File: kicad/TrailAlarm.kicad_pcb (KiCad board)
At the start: 2 copper layers, 71.1 x 36.2 mm, 57 parts, among them IC1 MAX865EUA+T, J1 Conn_01x03, J2 Conn_01x01_Male, J3 Adafruit ADS1115, J4 Bat, Q1 2N3904, SW1 SW_DIP_x01, U1 TLC274, U2 TL074, U3 PocketBeagle, U5 AD620

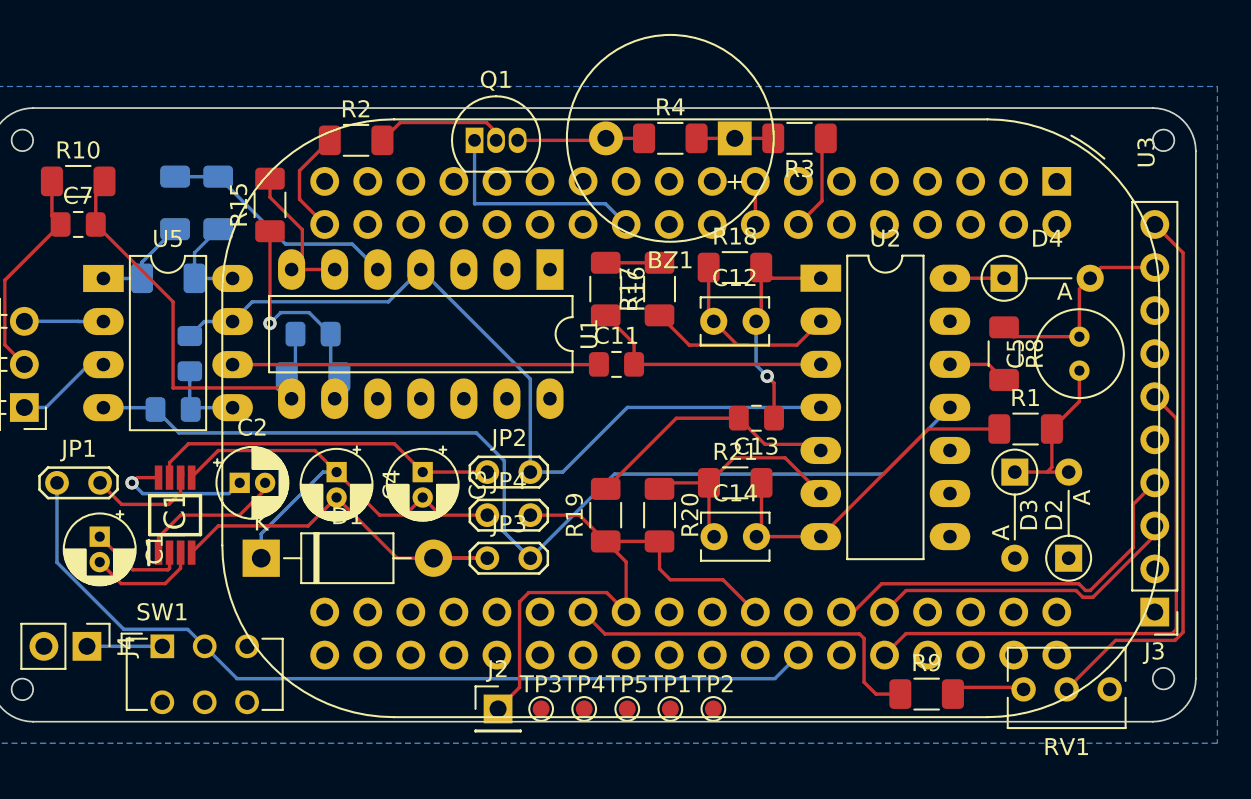
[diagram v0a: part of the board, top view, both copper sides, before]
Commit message: Done Layout
- Add paths for test points, better ground plane
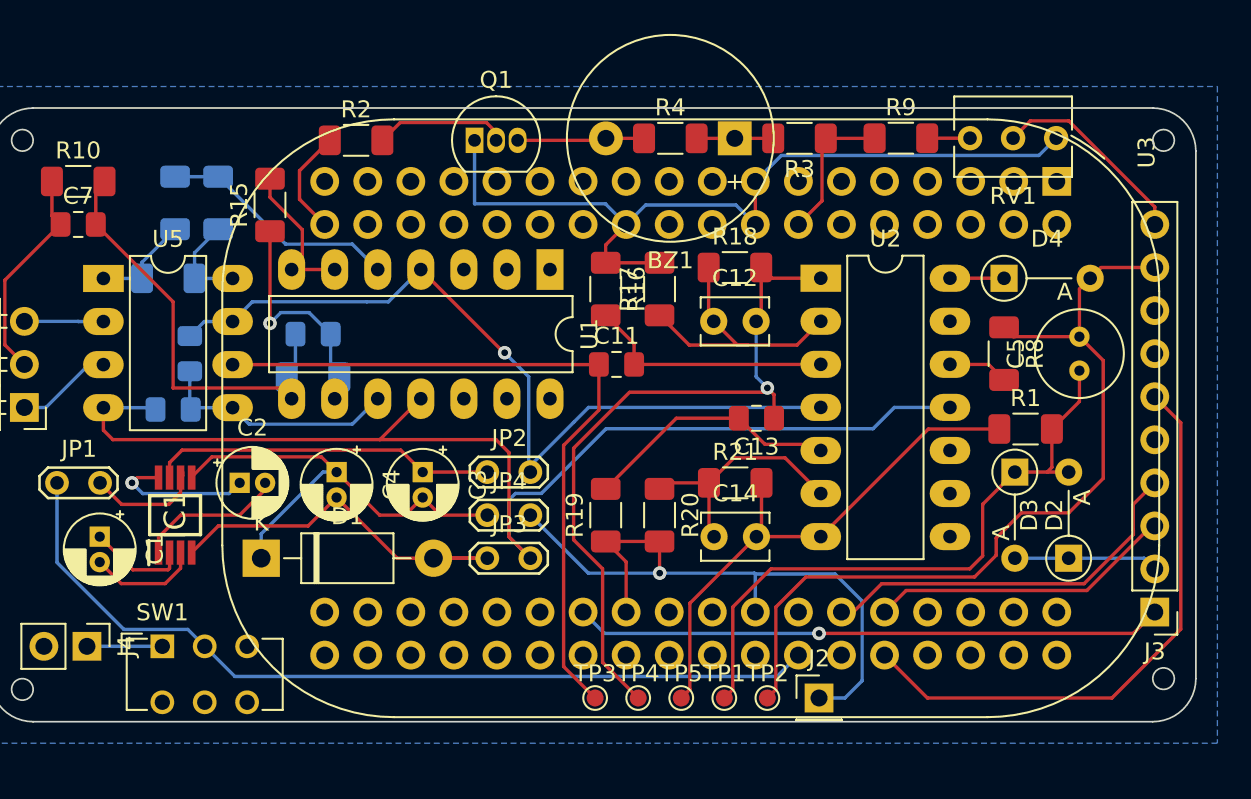
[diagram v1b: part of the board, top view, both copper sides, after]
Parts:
- moved R9 32.8 mm to (169.9, 14.5)
- moved RV1 32.7 mm to (174.0, 14.5)
- moved J2 18.9 mm to (165.1, 47.5)
- moved TP1 3.25 mm to (159.5, 47.5)
- moved TP2 3.25 mm to (162.1, 47.5)
- moved TP3 3.25 mm to (151.9, 47.5)
- moved TP4 3.25 mm to (154.4, 47.5)
- moved TP5 3.25 mm to (157.0, 47.5)
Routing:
- net GND: track 59.2 -> 113.6 mm, vias 0 -> 1
- net TO_ADC: track 12.8 -> 50.4 mm
- net Net-(C12-Pad2): track 13.2 -> 42.4 mm
- net Net-(C5-Pad1): track 10.3 -> 37.6 mm
- net Net-(C11-Pad1): track 21.6 -> 42.9 mm
- net Vref_mid: track 33.0 -> 11.9 mm
- net +3V3: track 28.0 -> 43.4 mm, vias 0 -> 1
- net VS: track 59.8 -> 71.3 mm
- net /EEG Amplifer/FullSignal: track 20.3 -> 31.6 mm
- net ~{ADC_RDY}: track 32.1 -> 34.5 mm
- net Vref_top: track 4.38 -> 2.53 mm
- net I2C_SDA: track 23.5 -> 22.7 mm
- net I2C_SCL: track 18.7 -> 18.0 mm
- net VD: track 48.6 -> 48.8 mm, vias 0 -> 1

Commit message: Export gerber files
- Reflow
- print to pdf
- generate gerber/drill files for fab
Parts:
- moved BZ1 99.8 mm to (160.8, 114.3)
- moved C1 99.8 mm to (123.4, 137.8)
- moved C11 99.8 mm to (153.9, 127.6)
- moved C12 99.8 mm to (159.6, 125.1)
- moved C14 99.8 mm to (159.6, 137.8)
- moved C3 99.8 mm to (142.4, 134.0)
- moved C4 99.8 mm to (137.4, 134.0)
- moved C7 99.8 mm to (122.1, 119.4)
- moved C8 99.8 mm to (136.0, 125.9)
- moved C9 99.8 mm to (128.7, 127.0)
- moved D1 99.8 mm to (132.9, 139.1)
- moved D2 99.8 mm to (177.4, 134.0)
- moved D3 99.8 mm to (180.5, 139.1)
- moved D4 99.8 mm to (176.7, 122.6)
- moved J1 99.8 mm to (118.9, 130.2)
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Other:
- outline, holes or cut-outs redrawn

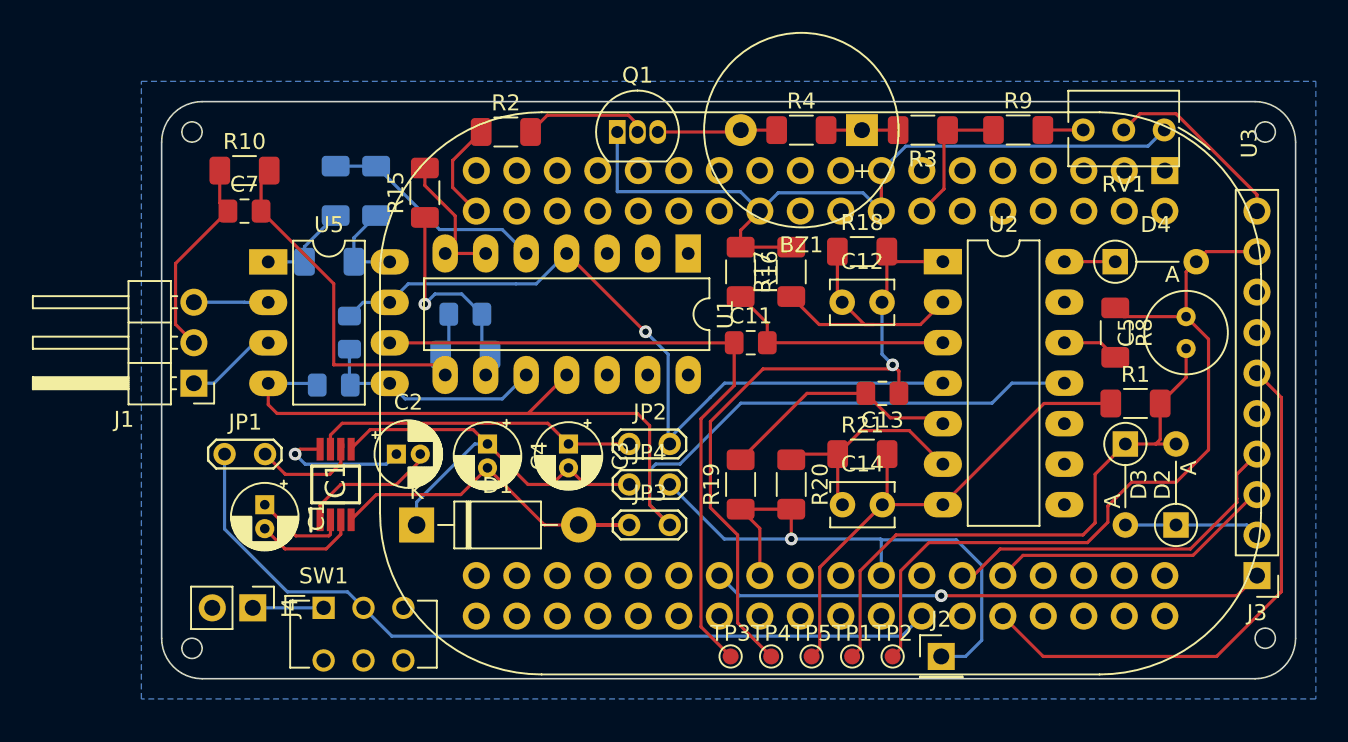
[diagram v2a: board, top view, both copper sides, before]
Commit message: Updated layout
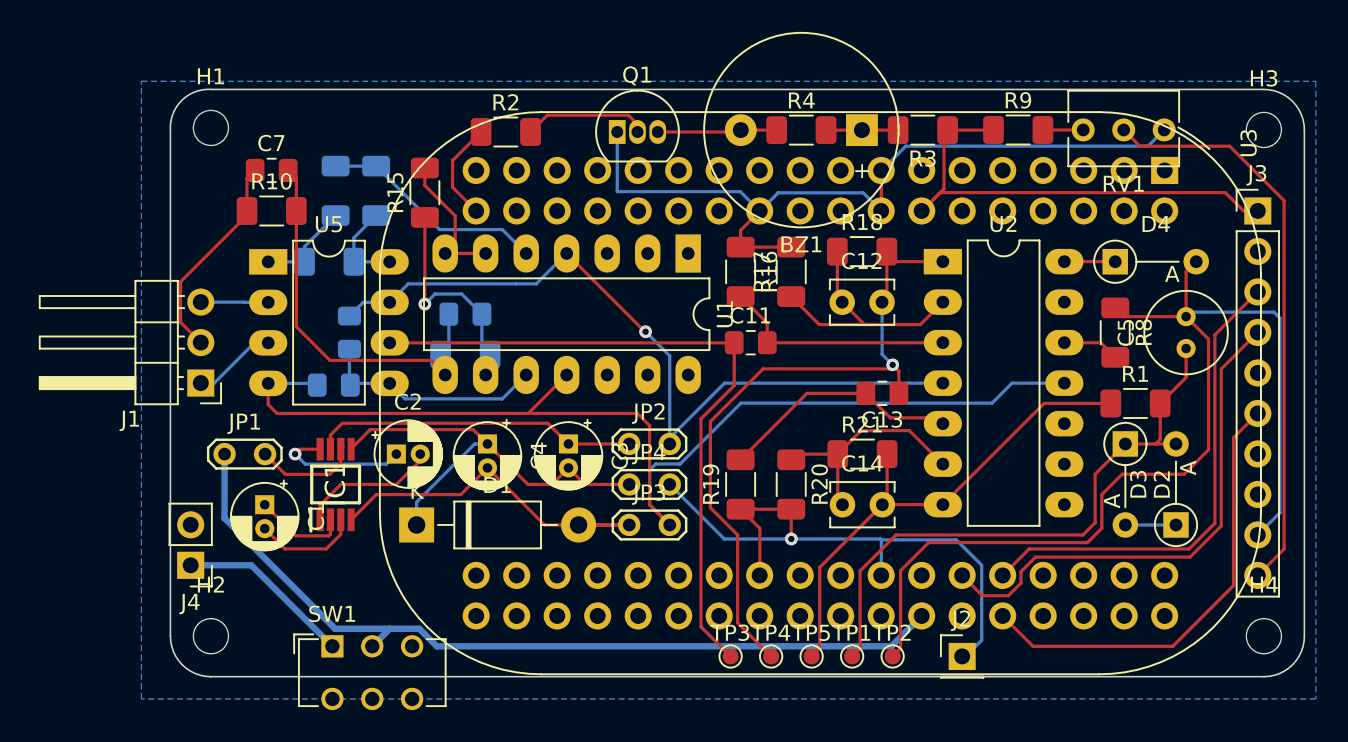
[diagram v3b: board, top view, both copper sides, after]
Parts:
- added H1: MountingHole, MountingHole:MountingHole_2.2mm_M2, F.Cu at (120.0, 114.2)
- added H2: MountingHole, MountingHole:MountingHole_2.2mm_M2, F.Cu at (120.0, 146.1)
- added H3: MountingHole, MountingHole:MountingHole_2.2mm_M2, F.Cu at (186.1, 114.3)
- added H4: MountingHole, MountingHole:MountingHole_2.2mm_M2, F.Cu at (186.1, 146.1)
- J1: value Conn_01x03 -> Electrodes
- moved J3 22.9 mm to (185.7, 119.4), turned to 0 degrees
- moved J4 4.72 mm to (118.7, 141.6), turned to 180 degrees
- moved C7 3.07 mm to (123.8, 116.8)
- moved R10 3.05 mm to (123.8, 119.4)
- moved SW1 2.48 mm to (127.6, 146.7)
- moved J2 1.31 mm to (167.1, 147.3)
- moved J1 0.43 mm to (119.4, 130.2)
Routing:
- net Vref_mid: track 11.9 -> 36.1 mm
- net TO_ADC: track 50.4 -> 67.3 mm
- net +3V3: track 43.4 -> 29.8 mm, vias 1 -> 0
- net I2C_SCL: track 18.0 -> 30.3 mm
- net I2C_SDA: track 22.7 -> 32.1 mm
- net GND: track 113.6 -> 106.8 mm
- net +BATT: track 4.44 -> 11.0 mm
- net ~{ADC_RDY}: track 34.5 -> 28.3 mm
- net POWER: track 51.7 -> 54.0 mm
- net Net-(C7-Pad2): track 25.7 -> 24.7 mm
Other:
- board size 71.1 x 36.2 mm -> 71.1 x 36.8 mm
